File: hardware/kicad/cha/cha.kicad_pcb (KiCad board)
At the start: 4 copper layers, 173 x 134 mm, 117 parts, among them J1 AES_CHA, J2 CONF C, J3 CONF SM, J4 Câble PROG-CHA, U1 AP63203WU, U10 74AHCT1G32, U11 74LVC1G07, U12 iCE40HX4K-TQ144, U13 AS4C32M16SB-6TIN, U14 iCE40HX4K-TQ144, U15 IS61WV10248EDBLL-10TLI, U2 AP2112K-1.2, U3 74LVC16244A, U4 74LVC16244A, U5 74LVC16244A, U6 74LVC16244A, U7 74AHCT16244, U8 74AHCT125, U9 74AHCT244, X1 25 MHz 3,3 V, X2 25 MHz 3,3 V

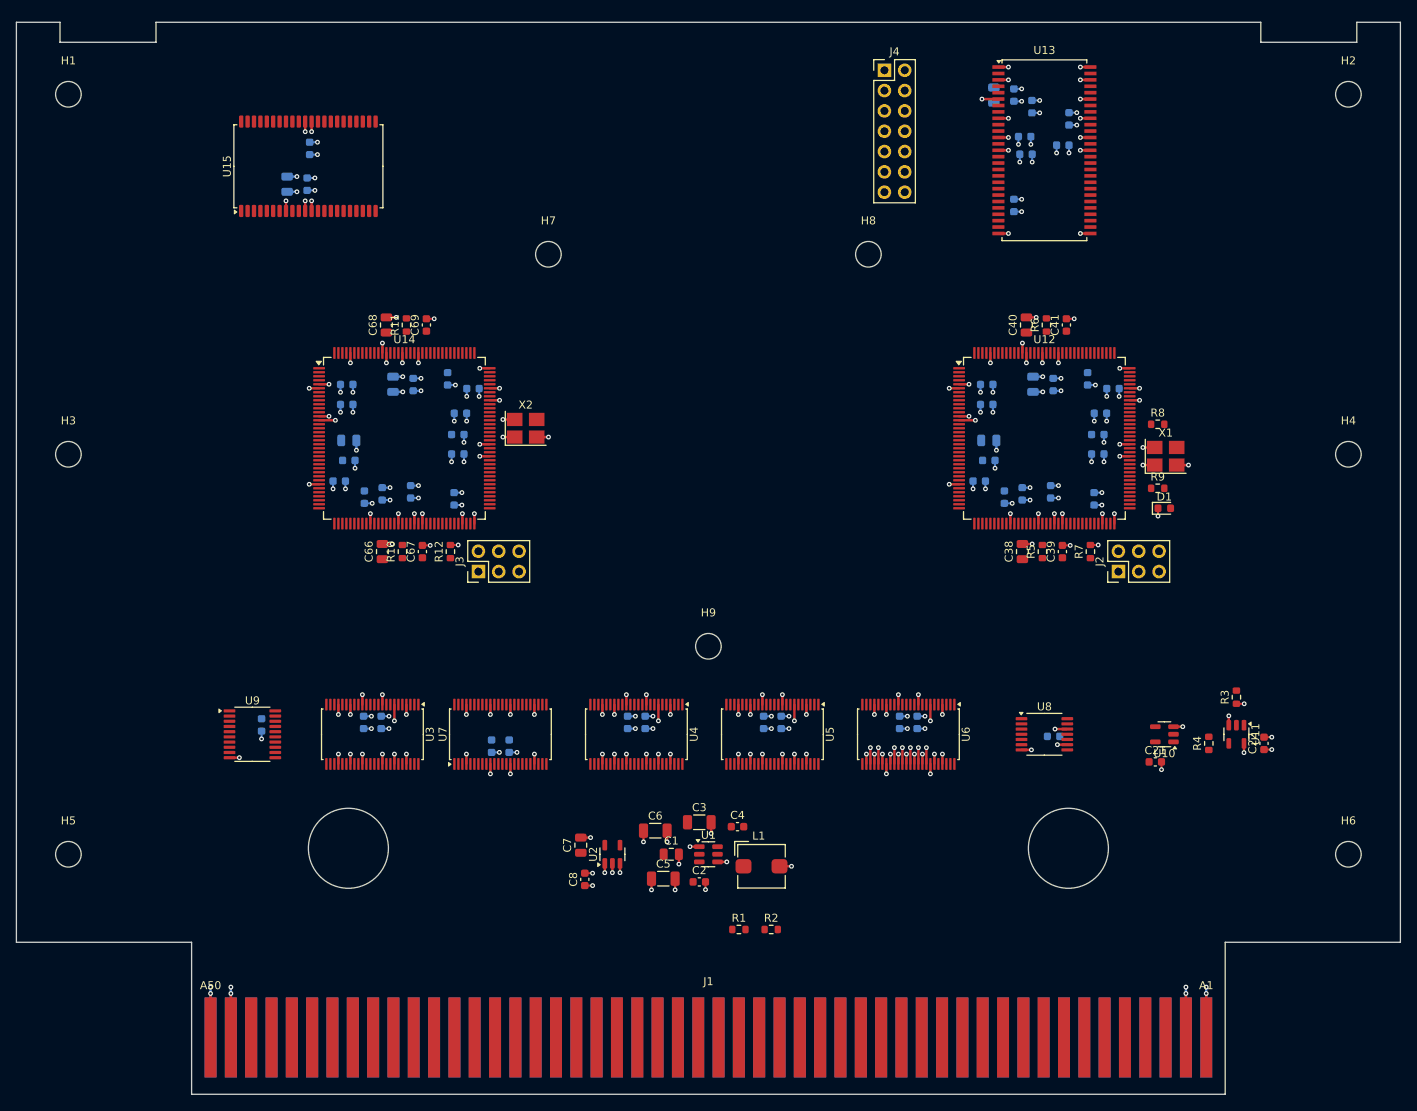
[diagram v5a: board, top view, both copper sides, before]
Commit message: Carte CHA routée : une seule liaison restante (SDA4)
Routage complet (régulateur à découpage, horloge SDRAM adaptée côté
FPGA, U8 en 74AHCT125) puis routeur de finition. DRC : aucune
violation de cuivre ; reste SDA4 (U14.37 -> U3.20).

Co-Authored-By: Claude Opus 5.5 <noreply@anthropic.com>
Claude-Session: https://claude.ai/code/session_01WKfXP1YJ8otGxZ5dsY6Agh
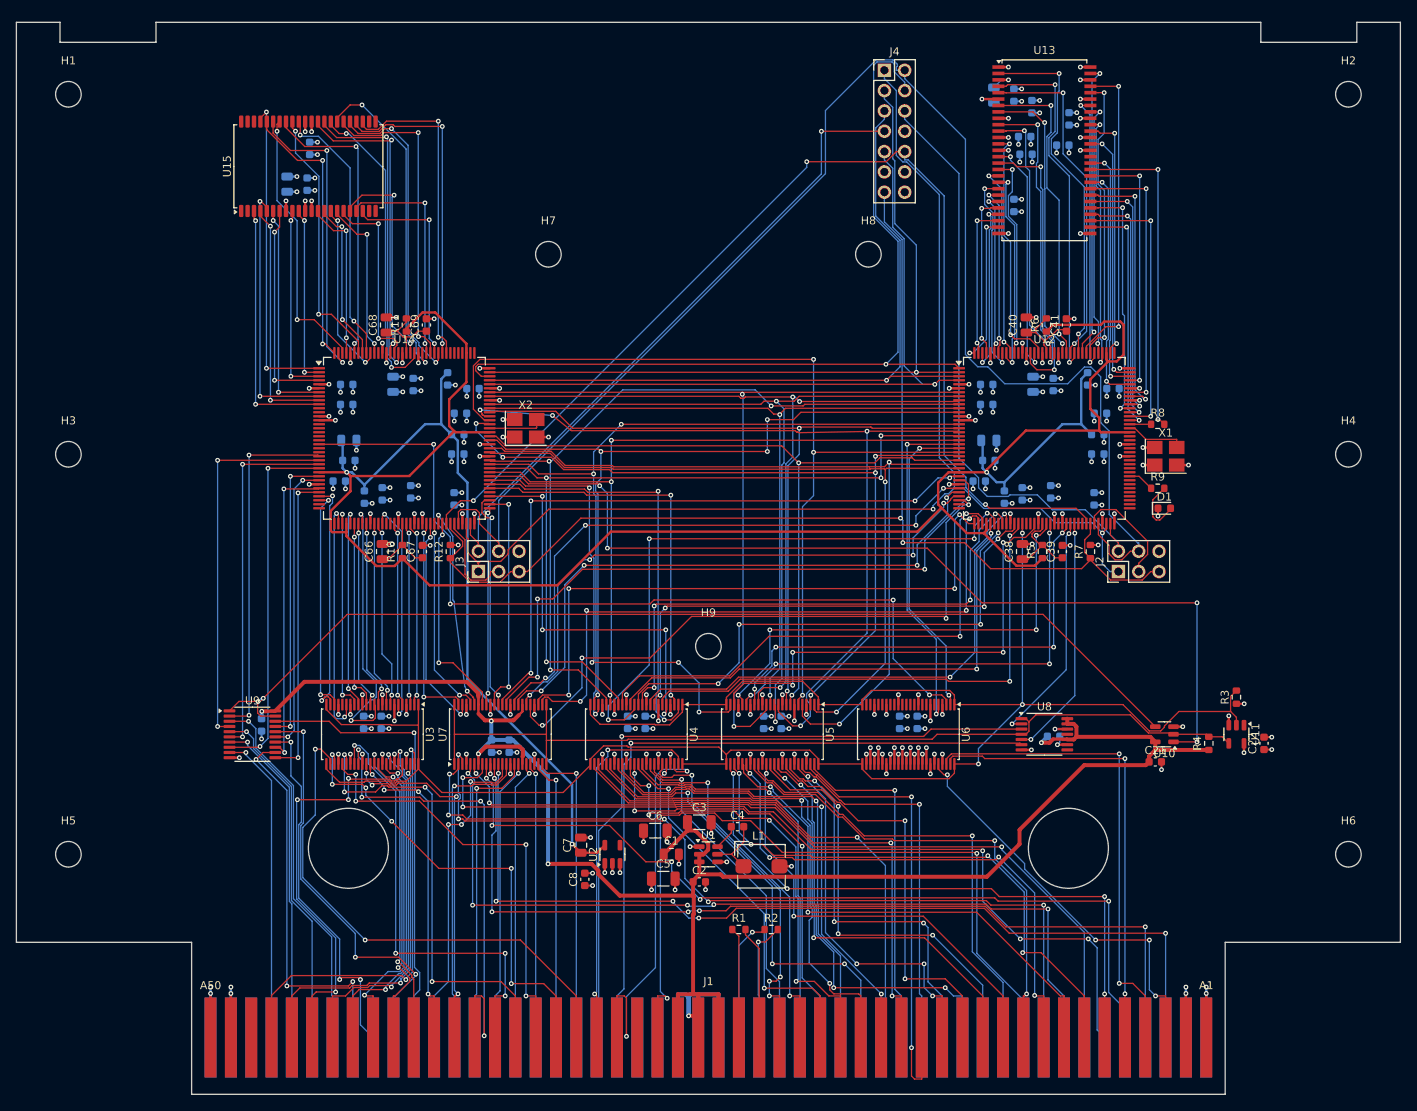
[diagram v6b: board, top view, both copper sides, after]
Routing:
- net +1V2: track 0.00 -> 335.4 mm, vias 0 -> 3
- net +5V: track 0.00 -> 263.2 mm, vias 0 -> 6
- net XLAT_EN_N: track 0.00 -> 249.0 mm, vias 0 -> 3
- net CHA_IO0: track 0.00 -> 187.0 mm
- net CHA_SCK: track 0.00 -> 155.2 mm, vias 0 -> 2
- net CRESET_N: track 0.00 -> 152.1 mm, vias 0 -> 2
- net CDONE: track 0.00 -> 140.3 mm, vias 0 -> 3
- net SDD_OE5_N: track 0.00 -> 131.0 mm, vias 0 -> 2
- net SDD_OE_N: track 0.00 -> 119.3 mm, vias 0 -> 4
- net AES_FIXD0: track 0.00 -> 116.7 mm, vias 0 -> 5
- net OE5_N: track 0.00 -> 116.2 mm
- net AES_FIXD1: track 0.00 -> 115.6 mm, vias 0 -> 5
- net P6: track 0.00 -> 113.0 mm, vias 0 -> 3
- net AES_FIXD3: track 0.00 -> 109.4 mm, vias 0 -> 5
- net CHA_IO2: track 0.00 -> 109.3 mm, vias 0 -> 1
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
